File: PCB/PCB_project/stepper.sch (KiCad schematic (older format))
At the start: 9 parts, among them J1 DB15_Female_HighDensity, J2 DB15_Female_HighDensity, J3 DB15_Female_HighDensity, U1 NUCLEO-L432KC, U2 AMIS-30543-POLOLU, U3 AMIS-30543-POLOLU, U4 AMIS-30543-POLOLU, U5 +12V, U6 GND

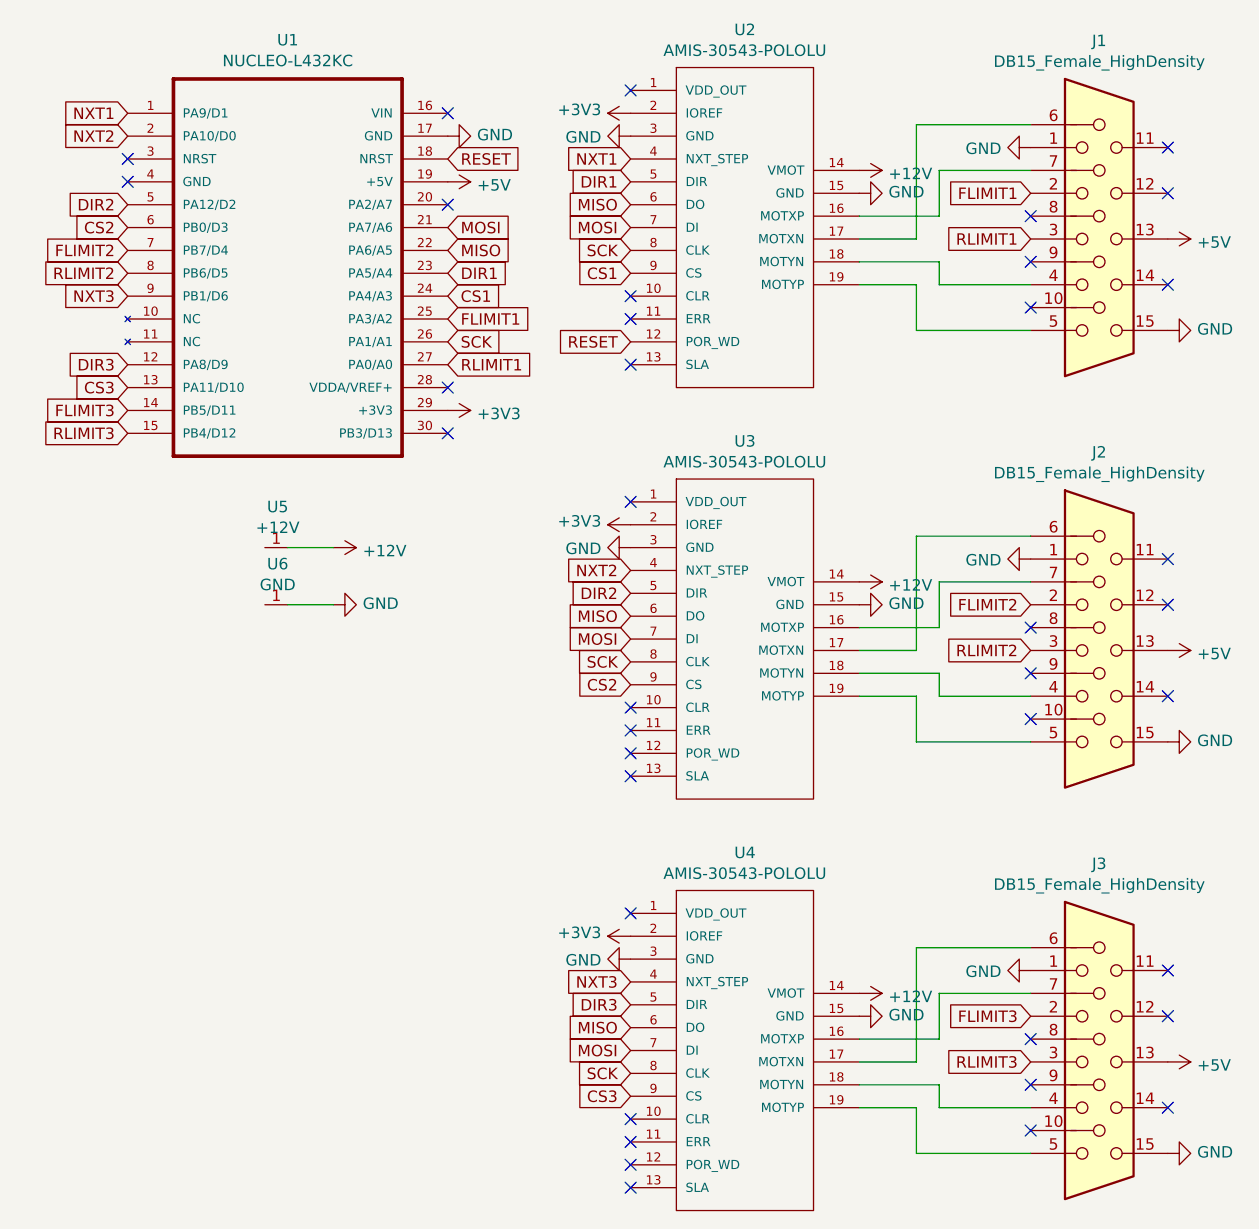
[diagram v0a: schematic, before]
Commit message: PCP updated after pin swap
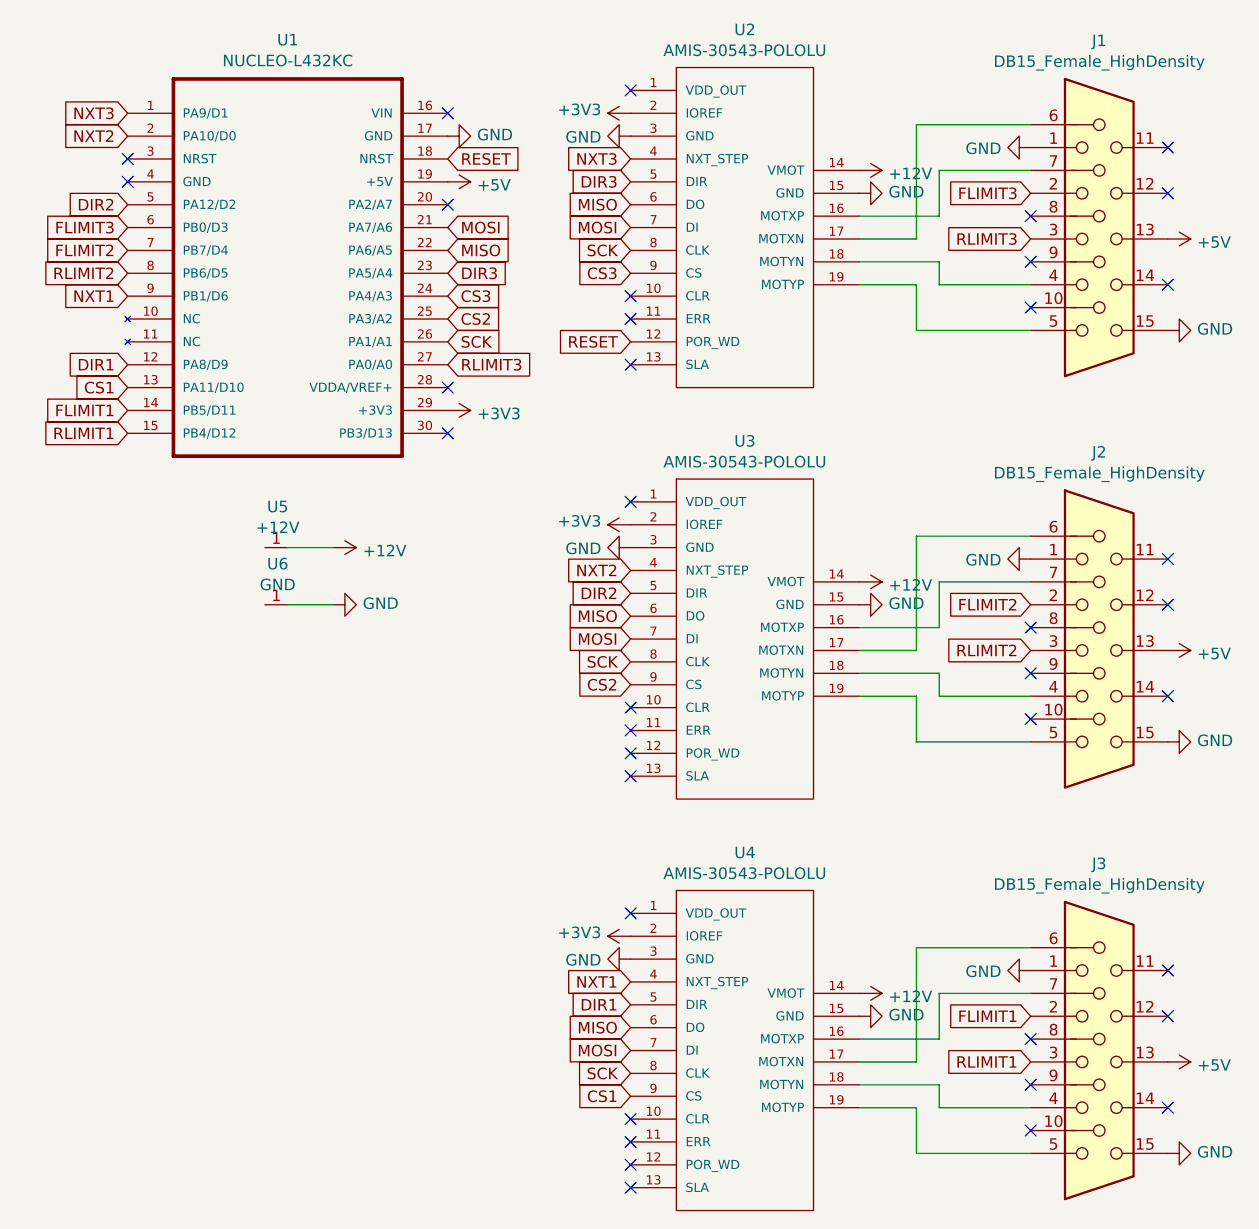
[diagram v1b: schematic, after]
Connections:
- net CS1: now also U1.13 (PA11/D10), U4.9 (CS); no longer U1.24 (PA4/A3), U2.9 (CS)
- net CS2: now also U1.25 (PA3/A2); no longer U1.6 (PB0/D3)
- net CS3: now also U1.24 (PA4/A3), U2.9 (CS); no longer U1.13 (PA11/D10), U4.9 (CS)
- net DIR1: now also U1.12 (PA8/D9), U4.5 (DIR); no longer U1.23 (PA5/A4), U2.5 (DIR)
- net DIR3: now also U1.23 (PA5/A4), U2.5 (DIR); no longer U1.12 (PA8/D9), U4.5 (DIR)
- net FLIMIT1: now also J3.2, U1.14 (PB5/D11); no longer J1.2, U1.25 (PA3/A2)
- net FLIMIT3: now also J1.2, U1.6 (PB0/D3); no longer J3.2, U1.14 (PB5/D11)
- net NXT1: now also U1.9 (PB1/D6), U4.4 (NXT_STEP); no longer U1.1 (PA9/D1), U2.4 (NXT_STEP)
- net NXT3: now also U1.1 (PA9/D1), U2.4 (NXT_STEP); no longer U1.9 (PB1/D6), U4.4 (NXT_STEP)
- net RLIMIT1: now also J3.3, U1.15 (PB4/D12); no longer J1.3, U1.27 (PA0/A0)
- net RLIMIT3: now also J1.3, U1.27 (PA0/A0); no longer J3.3, U1.15 (PB4/D12)
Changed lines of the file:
@@
 EESchema Schematic File Version 4
 LIBS:stepper-cache
-EELAYER 26 0
+EELAYER 30 0
 EELAYER END
 $Descr User 6378 7677
@@
 	0    -1   -1   0
 $EndComp
-Text GLabel 3100 1100 0    50   Input ~ 0
+Text GLabel 3100 4700 0    50   Input ~ 0
 NXT1
-Text GLabel 3100 1200 0    50   Input ~ 0
+Text GLabel 3100 4800 0    50   Input ~ 0
 DIR1
-Text GLabel 3100 1600 0    50   Input ~ 0
+Text GLabel 3100 5200 0    50   Input ~ 0
 CS1
-Text GLabel 4850 1250 0    50   Input ~ 0
+Text GLabel 4850 4850 0    50   Input ~ 0
 FLIMIT1
-Text GLabel 4850 1450 0    50   Input ~ 0
+Text GLabel 4850 5050 0    50   Input ~ 0
 RLIMIT1
 Text GLabel 3100 2900 0    50   Input ~ 0
@@
 Text GLabel 4850 3250 0    50   Input ~ 0
 RLIMIT2
-Text GLabel 4850 4850 0    50   Input ~ 0
+Text GLabel 4850 1250 0    50   Input ~ 0
 FLIMIT3
-Text GLabel 4850 5050 0    50   Input ~ 0
+Text GLabel 4850 1450 0    50   Input ~ 0
 RLIMIT3
-Text GLabel 3100 4700 0    50   Input ~ 0
+Text GLabel 3100 1100 0    50   Input ~ 0
 NXT3
-Text GLabel 3100 4800 0    50   Input ~ 0
+Text GLabel 3100 1200 0    50   Input ~ 0
 DIR3
-Text GLabel 3100 5200 0    50   Input ~ 0
+Text GLabel 3100 1600 0    50   Input ~ 0
 CS3
 $Comp
@@
 Wire Wire Line
 	1800 3050 1600 3050
-Text GLabel 900  900  0    50   Input ~ 0
+Text GLabel 900  1700 0    50   Input ~ 0
 NXT1
-Text GLabel 2300 1600 2    50   Input ~ 0
+Text GLabel 900  2000 0    50   Input ~ 0
 DIR1
-Text GLabel 2300 1700 2    50   Input ~ 0
+Text GLabel 900  2100 0    50   Input ~ 0
 CS1
-Text GLabel 2300 1800 2    50   Input ~ 0
+Text GLabel 900  2200 0    50   Input ~ 0
 FLIMIT1
-Text GLabel 2300 2000 2    50   Input ~ 0
+Text GLabel 900  2300 0    50   Input ~ 0
 RLIMIT1
 Text GLabel 2300 1900 2    50   Input ~ 0
@@
 Text GLabel 900  1300 0    50   Input ~ 0
 DIR2
-Text GLabel 900  1400 0    50   Input ~ 0
+Text GLabel 2300 1800 2    50   Input ~ 0
 CS2
 Text GLabel 900  1500 0    50   Input ~ 0
@@
 Text GLabel 900  1600 0    50   Input ~ 0
 RLIMIT2
-Text GLabel 900  1700 0    50   Input ~ 0
+Text GLabel 900  900  0    50   Input ~ 0
 NXT3
-Text GLabel 900  2000 0    50   Input ~ 0
+Text GLabel 2300 1600 2    50   Input ~ 0
 DIR3
-Text GLabel 900  2100 0    50   Input ~ 0
+Text GLabel 2300 1700 2    50   Input ~ 0
 CS3
-Text GLabel 900  2200 0    50   Input ~ 0
+Text GLabel 900  1400 0    50   Input ~ 0
 FLIMIT3
-Text GLabel 900  2300 0    50   Input ~ 0
+Text GLabel 2300 2000 2    50   Input ~ 0
 RLIMIT3
 NoConn ~ 2300 1300

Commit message: Adaptatations in pinout for future switch panel
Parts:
- added U7: EIN, TestPoint:TestPoint_Plated_Hole_D2.0mm, symbol stepper-rescue:WIREPAD-motor_driver
- added U8: +3V3, TestPoint:TestPoint_Plated_Hole_D2.0mm, symbol stepper-rescue:WIREPAD-motor_driver
- added U9: GND, TestPoint:TestPoint_Plated_Hole_D2.0mm, symbol stepper-rescue:WIREPAD-motor_driver
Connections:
- net +3V3: now also U8.1
- net CS2: now also U1.30 (PB3/D13); no longer U1.25 (PA3/A2)
- net GND: now also U9.1
- new net EIN: U1.25 (PA3/A2), U7.1
- no-connect marks 38 -> 37
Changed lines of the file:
@@
 Text GLabel 900  1300 0    50   Input ~ 0
 DIR2
-Text GLabel 2300 1800 2    50   Input ~ 0
+Text GLabel 2300 2300 2    50   Input ~ 0
 CS2
 Text GLabel 900  1500 0    50   Input ~ 0
@@
 NoConn ~ 2300 1300
 NoConn ~ 2300 2100
-NoConn ~ 2300 2300
 NoConn ~ 900  1100
 NoConn ~ 900  1200
@@
 NoConn ~ 4850 1350
 NoConn ~ 4850 1750
+$Comp
+L stepper-rescue:WIREPAD-motor_driver U7
+U 1 1 5EC2D357
+P 1600 3350
+F 0 "U7" H 1644 3172 50  0000 C CNN
+F 1 "EIN" H 1644 3263 50  0000 C CNN
+F 2 "TestPoint:TestPoint_Plated_Hole_D2.0mm" H 1600 3350 50  0001 C CNN
+F 3 "" H 1600 3350 50  0001 C CNN
+	1    1600 3350
+	-1   0    0    1
+$EndComp
+$Comp
+L stepper-rescue:WIREPAD-motor_driver U9
+U 1 1 5EC2DD93
+P 1600 3850
+F 0 "U9" H 1644 3672 50  0000 C CNN
+F 1 "GND" H 1644 3763 50  0000 C CNN
+F 2 "TestPoint:TestPoint_Plated_Hole_D2.0mm" H 1600 3850 50  0001 C CNN
+F 3 "" H 1600 3850 50  0001 C CNN
+	1    1600 3850
+	-1   0    0    1
+$EndComp
+$Comp
+L stepper-rescue:WIREPAD-motor_driver U8
+U 1 1 5EC2EA08
+P 1600 3600
+F 0 "U8" H 1644 3422 50  0000 C CNN
+F 1 "+3V3" H 1644 3513 50  0000 C CNN
+F 2 "TestPoint:TestPoint_Plated_Hole_D2.0mm" H 1600 3600 50  0001 C CNN
+F 3 "" H 1600 3600 50  0001 C CNN
+	1    1600 3600
+	-1   0    0    1
+$EndComp
+$Comp
+L stepper-rescue:GND-power #PWR0103
+U 1 1 5EC2EFF3
+P 1800 3850
+F 0 "#PWR0103" H 1800 3600 50  0001 C CNN
+F 1 "GND" V 1805 3722 50  0000 R CNN
+F 2 "" H 1800 3850 50  0001 C CNN
+F 3 "" H 1800 3850 50  0001 C CNN
+	1    1800 3850
+	0    -1   -1   0
+$EndComp
+$Comp
+L stepper-rescue:+3V3-power #PWR0128
+U 1 1 5EC2F830
+P 1800 3600
+F 0 "#PWR0128" H 1800 3450 50  0001 C CNN
+F 1 "+3V3" V 1815 3728 50  0000 L CNN
+F 2 "" H 1800 3600 50  0001 C CNN
+F 3 "" H 1800 3600 50  0001 C CNN
+	1    1800 3600
+	0    1    1    0
+$EndComp
+Text GLabel 2300 1800 2    50   Input ~ 0
+EIN
+Text GLabel 1800 3350 2    50   Input ~ 0
+EIN
+Wire Wire Line
+	1600 3350 1800 3350
+Wire Wire Line
+	1800 3600 1600 3600
+Wire Wire Line
+	1600 3850 1800 3850
 $EndSCHEMATC
